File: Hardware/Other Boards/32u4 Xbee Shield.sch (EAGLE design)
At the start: 20 parts, among them Q1 MOSFET-NCHANNELSMD, Q2 MOSFET-NCHANNELSMD, U2 XBEE-1B3, U3 V_REG_LDOSMD

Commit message: 32u4 Xbee Shield
32u4 Xbee Shield
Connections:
- net 5V: now also U$1.VCC
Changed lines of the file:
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@@
 <part name="P+6" library="SparkFun" deviceset="3.3V" device=""/>
 <part name="U$12" library="SparkFun" deviceset="5V" device=""/>
+<part name="U$4" library="SparkFun" deviceset="5V" device=""/>
 </parts>
 <sheets>
@@
 <instance part="P+6" gate="G$1" x="251.46" y="152.4"/>
 <instance part="U$12" gate="G$1" x="208.28" y="152.4"/>
+<instance part="U$4" gate="G$1" x="5.08" y="15.24" rot="R90"/>
 </instances>
 <busses>
@@
 <wire x1="139.7" y1="58.42" x2="139.7" y2="66.04" width="0.1524" layer="91"/>
 </segment>
+<segment>
+<pinref part="U$1" gate="G$1" pin="VCC"/>
+<pinref part="U$4" gate="G$1" pin="5V"/>
+</segment>
 </net>

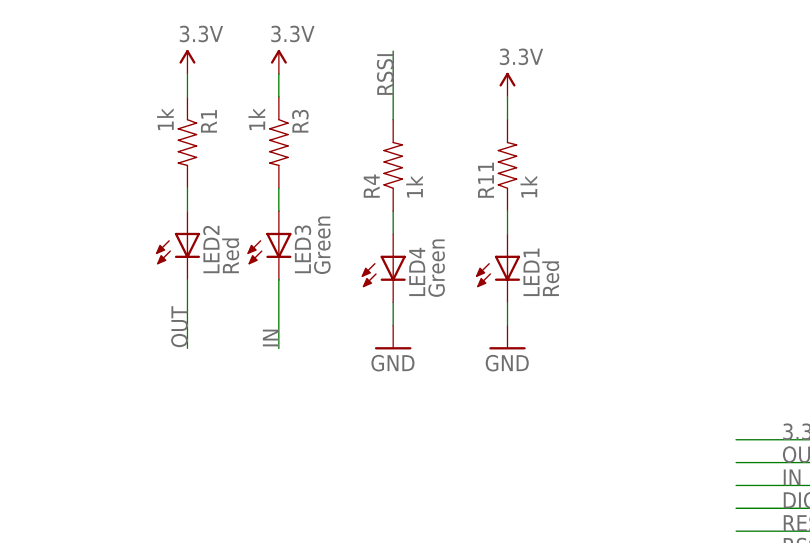
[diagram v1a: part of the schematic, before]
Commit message: Moved things around on xbee shield
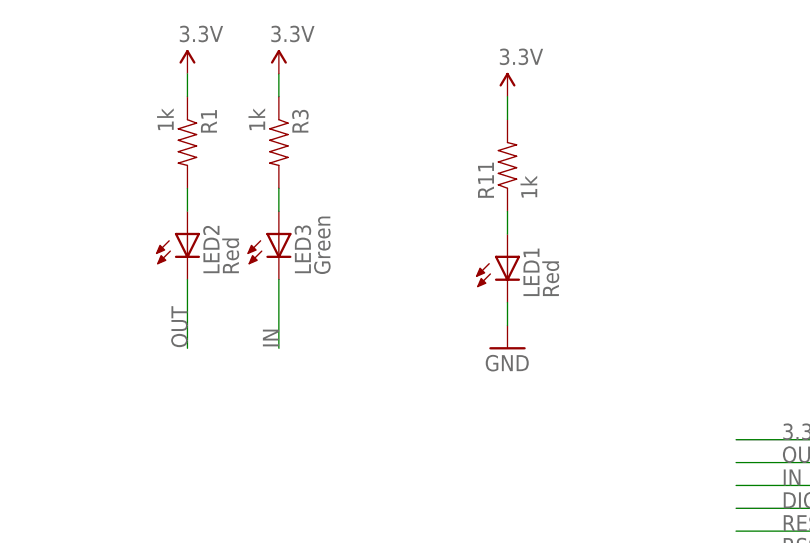
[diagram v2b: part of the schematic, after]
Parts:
- removed LED4: Green, SparkFun:LED0603
- removed R4: 1k, SparkFun-Passives:RESISTOR1206
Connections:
- removed net N$2: LED4.A, R4.1
- net GND: no longer LED4.C
- net RSSI: no longer R4.2
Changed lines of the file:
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@@
 <part name="P+1" library="SparkFun" deviceset="3.3V" device=""/>
 <part name="GND3" library="SparkFun" deviceset="GND" device=""/>
-<part name="LED4" library="SparkFun" deviceset="LED" device="0603" value="Green"/>
-<part name="R4" library="SparkFun-Passives" deviceset="RESISTOR" device="1206" value="1k"/>
-<part name="GND4" library="SparkFun" deviceset="GND" device=""/>
 <part name="U3" library="SparkFun" deviceset="V_REG_LDO" device="SMD"/>
 <part name="GND5" library="SparkFun" deviceset="GND" device=""/>
@@
 <instance part="P+1" gate="G$1" x="137.16" y="121.92"/>
 <instance part="GND3" gate="1" x="137.16" y="91.44"/>
-<instance part="LED4" gate="G$1" x="76.2" y="139.7"/>
-<instance part="R4" gate="G$1" x="76.2" y="149.86" rot="R90"/>
-<instance part="GND4" gate="1" x="76.2" y="129.54"/>
 <instance part="U3" gate="G$1" x="231.14" y="144.78" smashed="yes">
 <attribute name="NAME" x="223.52" y="153.924" size="1.778" layer="95"/>
@@
 </segment>
 <segment>
-<wire x1="76.2" y1="134.62" x2="76.2" y2="132.08" width="0.1524" layer="91"/>
-<pinref part="LED4" gate="G$1" pin="C"/>
-<pinref part="GND4" gate="1" pin="GND"/>
-</segment>
-<segment>
 <wire x1="220.98" y1="144.78" x2="215.9" y2="144.78" width="0.1524" layer="91"/>
 <wire x1="215.9" y1="144.78" x2="215.9" y2="137.16" width="0.1524" layer="91"/>
@@
 <pinref part="U2" gate="G$1" pin="RSSI"/>
 </segment>
-<segment>
-<wire x1="76.2" y1="154.94" x2="76.2" y2="162.56" width="0.1524" layer="91"/>
-<label x="76.2" y="157.48" size="1.778" layer="95" rot="R90"/>
-<pinref part="R4" gate="G$1" pin="2"/>
-</segment>
 </net>
 <net name="DIO12" class="0">
@@
 </segment>
 </net>
-<net name="N$2" class="0">
-<segment>
-<wire x1="76.2" y1="144.78" x2="76.2" y2="142.24" width="0.1524" layer="91"/>
-<pinref part="LED4" gate="G$1" pin="A"/>
-<pinref part="R4" gate="G$1" pin="1"/>
-</segment>
-</net>
